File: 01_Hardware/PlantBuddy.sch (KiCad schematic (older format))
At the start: 52 parts, among them J1 SWD, J2 Conn_I2C_SDA, J3 Conn_I2C_SCL, Q1 AO3401, Q2 AO3400A, SW1 PWR_SW, SW2 BLE_RST_SW, U1 OPT3001, U3 LMC555xM, U5 BlueNRG-M1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

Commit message: Switched to nRF52810.
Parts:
- removed C18: 2.2pF, Capacitor_SMD:C_0402_1005Metric, symbol Device:C_Small
- removed C19, C20: 1.5pF, Capacitor_SMD:C_0402_1005Metric, symbol Device:C_Small
- removed C22, C23: 2pF, Capacitor_SMD:C_0402_1005Metric, symbol Device:C_Small
- removed C26: 20pF, Capacitor_SMD:C_0402_1005Metric, symbol Device:C_Small
- removed L2: 2.7nH, Inductor_SMD:L_0402_1005Metric, symbol Device:L_Small
- removed L3: 3.3nH, Inductor_SMD:L_0402_1005Metric, symbol Device:L_Small
- removed R13: 10k, Resistor_SMD:R_0402_1005Metric, symbol Device:R_Small
- removed SW1: PWR_SW, Button_Switch_SMD:SW_SPDT_CK-JS102011SAQN, symbol Switch:SW_SPDT
- removed U5: BlueNRG-M1, Package_DFN_QFN:QFN-32-1EP_5x5mm_P0.5mm_EP3.3x3.3mm_ThermalVias, symbol PlantBuddy:BlueNRG-M1
- added C15: 4.7uF, Capacitor_SMD:C_0402_1005Metric, symbol Device:C_Small
- added C17: 100nF, Capacitor_SMD:C_0402_1005Metric, symbol Device:C_Small
- added U2: nRF52810-QCxx, Package_DFN_QFN:QFN-32-1EP_5x5mm_P0.5mm_EP3.6x3.6mm_ThermalVias, symbol MCU_Nordic:nRF52810-QCxx
- C13, C14: value 20pF -> 12pF; LCSC C1554 -> C1547
- C7: value 100nF -> 1.2pF; LCSC C1525 -> C159809
- C8: value 22uF -> 0.8pF; footprint Capacitor_SMD:C_0603_1608Metric -> Capacitor_SMD:C_0402_1005Metric; LCSC C59461 -> C326068
- C9: value 100nF -> 100pF; LCSC C1525 -> C1546
- J1: footprint PlantBuddy:Debug_Connector -> Connector_PinHeader_2.54mm:PinHeader_1x04_P2.54mm_Vertical
- J2, J3: footprint TestPoint:TestPoint_Pad_D1.5mm -> TestPoint:TestPoint_Pad_D1.0mm
- L1: value 2.7nH -> 3.9nH; LCSC C27123 -> C14033
- Y1: value 16MHz -> 32MHz; LCSC C13738 -> C90934
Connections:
- net labels added: XC1, XC2, XL1, XL2
- net labels removed: FXTAL0, FXTAL1, SXTAL0, SXTAL1
- wire segments 136 -> 105
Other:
- note added: "ADC configured with internal reference\nand gain 1/6 => 0 - 3.6V"
- note added: "Fuck BlueNRG."
- note added: "Pin32"
- note added: "TODO:\nPut it in such a way that\n it is small and hidden\nWe will need to build \na programming rig for it!"
- note removed: "50Ω matched trace"
- note removed: "ADC can be configured to\ninternally sense VBat"
- note removed: "Added SMPS\nfor minimum\npower"
- note removed: "Balun\n25.4Ω to 50Ω"
- note removed: "DC blocking"
- note removed: "Ideal values:\nL = 2.3nH\nC = 1.8pF"
- note removed: "Impedance matching to 25.4Ω\nby subtracting imaginary part\n"
- note removed: "Low-power reverse voltage protection\n& shutdown switch"
- note removed: "N3: DO NOT debug with battery connected!"
- note removed: "N4: The BlueNRG has an internal temperature sensor"
- note removed: "Put it in such a way that\n it is small and hidden\nWe will need to build \na programming rig for it!"
- note removed: "RoT: ~~0.3pF per PAD"
- note removed: "Should be ~~3.1pF\nbut considering\nparasitic capacitances\nwe chose this value"
- note removed: "VSWR with current design: ~~1.4\n"
- note removed: "^PI Low-pass Filter @ 2.45GHz"
- moved on the sheet: AE1, C10, C11, C12, C13, C14, C16, C5, C6, L4, R12, Y1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

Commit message: Slight hardware changes.
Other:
- note added: "TODO: Muta reset btn-ul mai sus, altfel nu il pot\naccesa din cauza pamantului"
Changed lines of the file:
@@
 Wire Bus Line
 	2150 4500 2150 5825
+Text Notes 7550 6350 0    50   ~ 0
+TODO: Muta reset btn-ul mai sus, altfel nu il pot\naccesa din cauza pamantului
 $EndSCHEMATC

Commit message: Revised 3d models a bit
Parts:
- AE1: symbol Device:Antenna_Shield -> PlantBuddy-rescue:Antenna_Shield-Device
- BT1: symbol Device:Battery_Cell -> PlantBuddy-rescue:Battery_Cell-Device
- C1, C10, C11, C12, C13, C14, C15, C16, C17, C2, C3, C4, C5, C6, C7, C8, C9: symbol Device:C_Small -> PlantBuddy-rescue:C_Small-Device
- D1, D2: symbol Device:LED_Small -> PlantBuddy-rescue:LED_Small-Device
- J1: symbol Connector_Generic:Conn_01x04 -> PlantBuddy-rescue:Conn_01x04-Connector_Generic
- J2, J3: symbol Connector_Generic:Conn_01x01 -> PlantBuddy-rescue:Conn_01x01-Connector_Generic
- L1, L4: symbol Device:L_Small -> PlantBuddy-rescue:L_Small-Device
- Q1: symbol Transistor_FET:AO3401A -> PlantBuddy-rescue:AO3401A-Transistor_FET
- Q2: symbol Device:Q_NMOS_GSD -> PlantBuddy-rescue:Q_NMOS_GSD-Device
- R1, R12, R14, R15, R16, R2, R3, R8, R9: symbol Device:R_Small -> PlantBuddy-rescue:R_Small-Device
- SW2: symbol Switch:SW_Push -> PlantBuddy-rescue:SW_Push-Switch
- U2: symbol MCU_Nordic:nRF52810-QCxx -> PlantBuddy-rescue:nRF52810-QCxx-MCU_Nordic
- U3: symbol Timer:LMC555xM -> PlantBuddy-rescue:LMC555xM-Timer
- U6: symbol Sensor_Humidity:SHTC3 -> PlantBuddy-rescue:SHTC3-Sensor_Humidity
- Y1: symbol Device:Crystal_GND24_Small -> PlantBuddy-rescue:Crystal_GND24_Small-Device
- Y2: symbol Device:Crystal_Small -> PlantBuddy-rescue:Crystal_Small-Device

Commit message: Slight PCB modifications
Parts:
- removed D2: R, LED_SMD:LED_0603_1608Metric, symbol PlantBuddy-rescue:LED_Small-Device
- removed R12: 10k, Resistor_SMD:R_0402_1005Metric, symbol PlantBuddy-rescue:R_Small-Device
- removed R16: 1k, Resistor_SMD:R_0402_1005Metric, symbol PlantBuddy-rescue:R_Small-Device
- removed SW2: BLE_RST_SW, Button_Switch_SMD:SW_SPST_EVQP7C, symbol PlantBuddy-rescue:SW_Push-Switch
- added R4: 10k, Resistor_SMD:R_0402_1005Metric, symbol PlantBuddy-rescue:R_Small-Device
- J1: value SWD -> SWD+DBG; footprint Connector_PinHeader_2.54mm:PinHeader_1x04_P2.54mm_Vertical -> Connector_PinHeader_2.54mm:PinHeader_2x03_P2.54mm_Vertical; symbol PlantBuddy-rescue:Conn_01x04-Connector_Generic -> Connector_Generic:Conn_02x03_Odd_Even
- L4: LCSC C1046 -> C95978
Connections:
- net +BATT: now also R4.1; no longer Q2.1 (G)
- net GND: now also J1.6 (Pin_6); no longer J1.4 (Pin_4)
- net LEDY: now also U2.10 (P0.12); no longer U2.15 (P0.20)
- net SWCLK: now also J1.3 (Pin_3); no longer J1.2 (Pin_2)
- net SWDIO: now also J1.5 (Pin_5); no longer J1.3 (Pin_3)
- net at U2.16 (P0.21/~RESET): now also R1.2
- net LEDR renamed UART_Rx
- net UART_Rx: now also J1.2 (Pin_2)
- net ~BLE_RST: no longer names the net of U2.11 (P0.14)
- net ~BLE_RST: no longer R1.2
- new net: Q2.1 (G), R4.2
- new net UART_Tx: J1.4 (Pin_4), U2.15 (P0.20)
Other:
- note removed: "A really small cheap button to be used\nfor resetting the bluetooth connection\nor reset to default settings"
- note removed: "TODO: Muta reset btn-ul mai sus, altfel nu il pot\naccesa din cauza pamantului"
- note removed: "TODO:\nPut it in such a way that\n it is small and hidden\nWe will need to build \na programming rig for it!"
- moved on the sheet: BT1, Q2

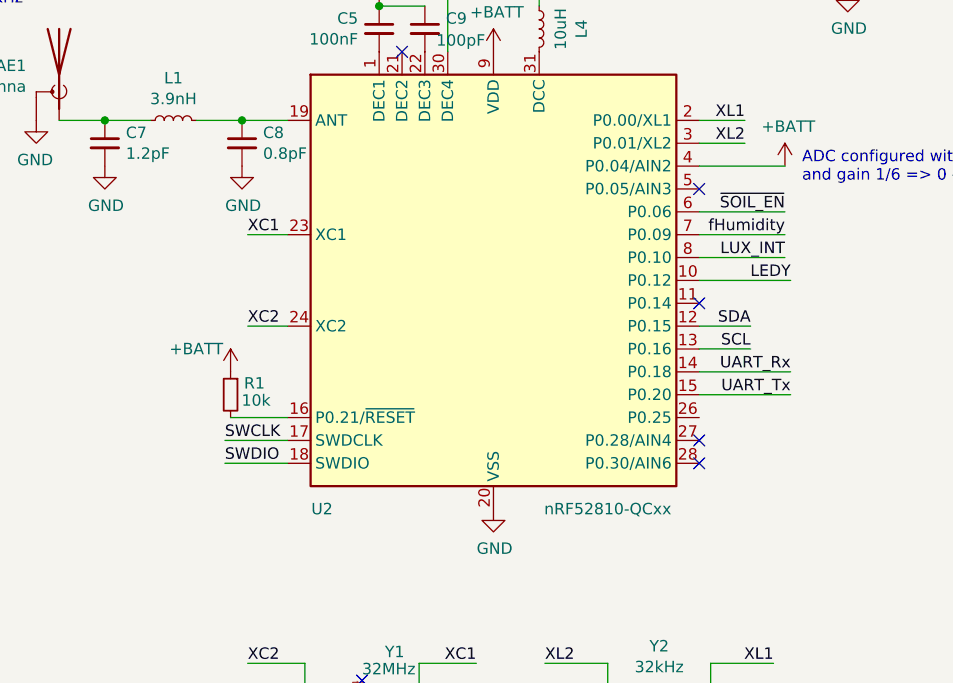
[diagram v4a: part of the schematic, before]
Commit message: Changed to two-layer PCB
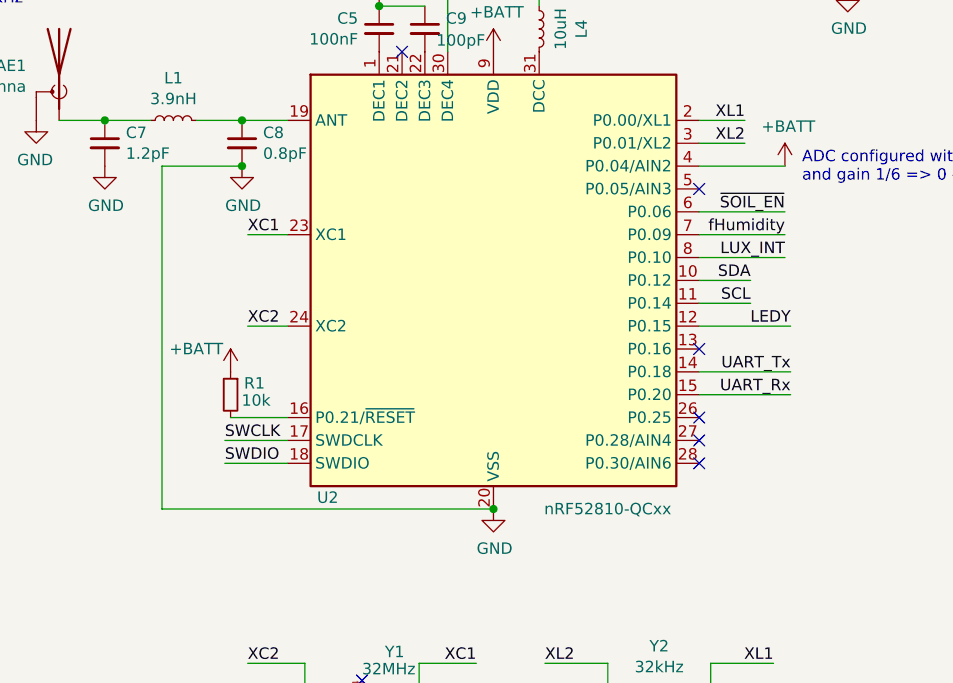
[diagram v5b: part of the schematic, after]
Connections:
- net LEDY: now also U2.12 (P0.15); no longer U2.10 (P0.12)
- net SCL: now also U2.11 (P0.14); no longer U2.13 (P0.16)
- net SDA: now also U2.10 (P0.12); no longer U2.12 (P0.15)
- net UART_Rx: now also U2.15 (P0.20); no longer U2.14 (P0.18)
- net UART_Tx: now also U2.14 (P0.18); no longer U2.15 (P0.20)
- no-connect marks 7 -> 8
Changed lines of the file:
@@
 Text Label 8425 2875 2    50   ~ 0
 fHumidity
-Text Label 8275 3375 2    50   ~ 0
+Text Label 8275 3175 2    50   ~ 0
 SCL
-Text Label 8275 3275 2    50   ~ 0
+Text Label 8275 3075 2    50   ~ 0
 SDA
 Wire Wire Line
@@
 $EndComp
 Wire Wire Line
-	8275 3375 8050 3375
-Wire Wire Line
-	8275 3275 8050 3275
+	8275 3175 8050 3175
+Wire Wire Line
+	8275 3075 8050 3075
 Wire Wire Line
 	7350 1875 7350 1800
@@
 Text Label 8425 2975 2    50   ~ 0
 LUX_INT
-Text Label 8450 3075 2    50   ~ 0
+Text Label 8450 3275 2    50   ~ 0
 LEDY
 Wire Wire Line
@@
 	875  4600 875  4800
 Wire Wire Line
-	8050 3075 8450 3075
+	8050 3275 8450 3275
 $Comp
 L PlantBuddy-rescue:nRF52810-QCxx-MCU_Nordic U2
 U 1 1 601392C1
 P 7150 3075
-F 0 "U2" H 6400 2075 50  0000 C CNN
+F 0 "U2" H 6425 2125 50  0000 C CNN
 F 1 "nRF52810-QCxx" H 7650 2075 50  0000 C CNN
 F 2 "Package_DFN_QFN:QFN-32-1EP_5x5mm_P0.5mm_EP3.6x3.6mm_ThermalVias" H 7150 1725 50  0001 C CNN
@@
 $EndComp
 Wire Wire Line
+	8050 3575 8450 3575
+Wire Wire Line
 	8050 3475 8450 3475
-Wire Wire Line
-	8050 3575 8450 3575
+Text Label 8450 3575 2    50   ~ 0
+UART_Rx
 Text Label 8450 3475 2    50   ~ 0
-UART_Rx
-Text Label 8450 3575 2    50   ~ 0
 UART_Tx
-NoConn ~ 8050 3175
 $Comp
 L PlantBuddy-rescue:R_Small-Device R4
@@
 Wire Wire Line
 	10550 800  10875 800
+Connection ~ 6050 2575
+Wire Wire Line
+	5700 2575 5700 4075
+Connection ~ 7150 4075
+Wire Wire Line
+	5700 4075 7150 4075
+Wire Wire Line
+	5700 2575 6050 2575
+NoConn ~ 8050 3375
+NoConn ~ 8050 3675
 Wire Bus Line
 	2150 4500 2600 4500

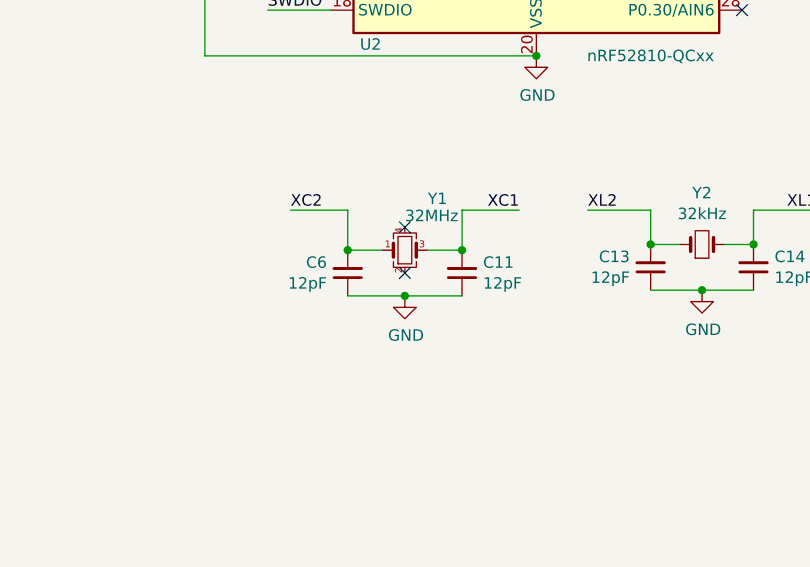
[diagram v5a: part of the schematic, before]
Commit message: Slight modifications to two-layer version
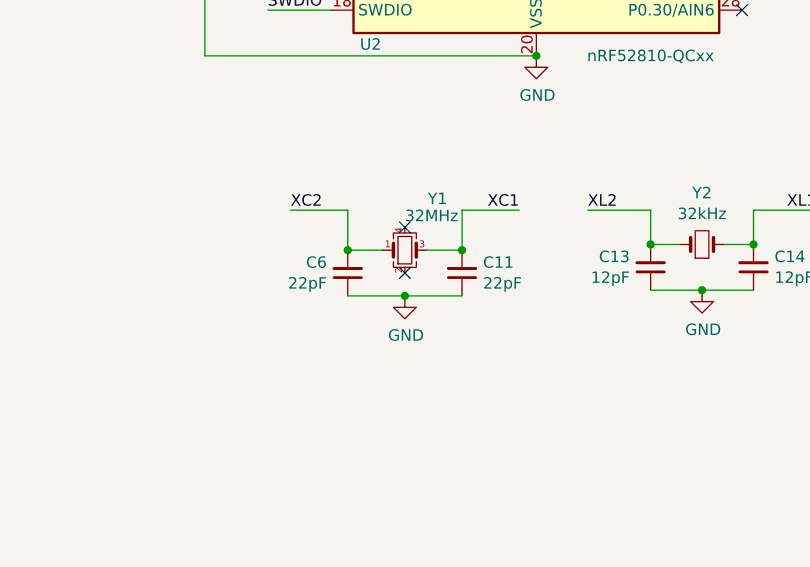
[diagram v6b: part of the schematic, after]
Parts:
- C11, C6: value 12pF -> 22pF
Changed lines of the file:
@@
 P 6825 5025
 F 0 "C11" H 6733 4979 50  0000 R CNN
-F 1 "12pF" H 6733 5070 50  0000 R CNN
+F 1 "22pF" H 6733 5070 50  0000 R CNN
 F 2 "Capacitor_SMD:C_0402_1005Metric" H 6825 5025 50  0001 C CNN
 F 3 "https://datasheet.lcsc.com/szlcsc/Guangdong-Fenghua-Advanced-Tech-0402CG120J500NT_C1547.pdf" H 6825 5025 50  0001 C CNN
@@
 P 6325 5025
 F 0 "C6" H 6234 4979 50  0000 R CNN
-F 1 "12pF" H 6234 5070 50  0000 R CNN
+F 1 "22pF" H 6234 5070 50  0000 R CNN
 F 2 "Capacitor_SMD:C_0402_1005Metric" H 6325 5025 50  0001 C CNN
 F 3 "https://datasheet.lcsc.com/szlcsc/Guangdong-Fenghua-Advanced-Tech-0402CG120J500NT_C1547.pdf" H 6325 5025 50  0001 C CNN
